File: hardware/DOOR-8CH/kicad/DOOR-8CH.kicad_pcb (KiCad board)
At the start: 4 copper layers, 260 x 160 mm, 230 parts, among them J1 FUSED_12V_CH1, J10 ACTUATOR_CH2, J11 ACTUATOR_CH3, J12 ACTUATOR_CH4, J13 ACTUATOR_CH5, J14 ACTUATOR_CH6, J15 ACTUATOR_CH7, J16 ACTUATOR_CH8, J2 FUSED_12V_CH2, J201 REED_A_OPEN_3V3_SIG_GND, J202 REED_A_CLOSED_3V3_SIG_GND, J203 REED_A_IN_PLACE_3V3_SIG_GND, J204 REED_B_OPEN_3V3_SIG_GND, J205 REED_B_CLOSED_3V3_SIG_GND, J206 REED_B_IN_PLACE_3V3_SIG_GND, J211 CAP_CS1_GND, J212 CAP_CS2_GND, J213 CAP_CS3_GND, J214 CAP_CS4_GND, J215 CAP_CS5_GND, J216 CAP_CS6_GND, J217 CAP_CS7_GND, J218 CAP_CS8_GND, J220 SWD_S1_3V3_DIO_CLK_NRST_GND, J230 LOGIC_12V_GND, J240 CANH_CANL_GND_SHIELD, J3 FUSED_12V_CH3, J4 FUSED_12V_CH4, J5 FUSED_12V_CH5, J6 FUSED_12V_CH6, J7 FUSED_12V_CH7, J8 FUSED_12V_CH8, J9 ACTUATOR_CH1, U1 VNH5019A-E, U2 VNH5019A-E, U230 AMS1117-3V3, U250 25LC256_SOIC8_CARRIER_ID, U3 VNH5019A-E, U4 VNH5019A-E, U5 VNH5019A-E, U6 VNH5019A-E, U7 VNH5019A-E, U8 VNH5019A-E

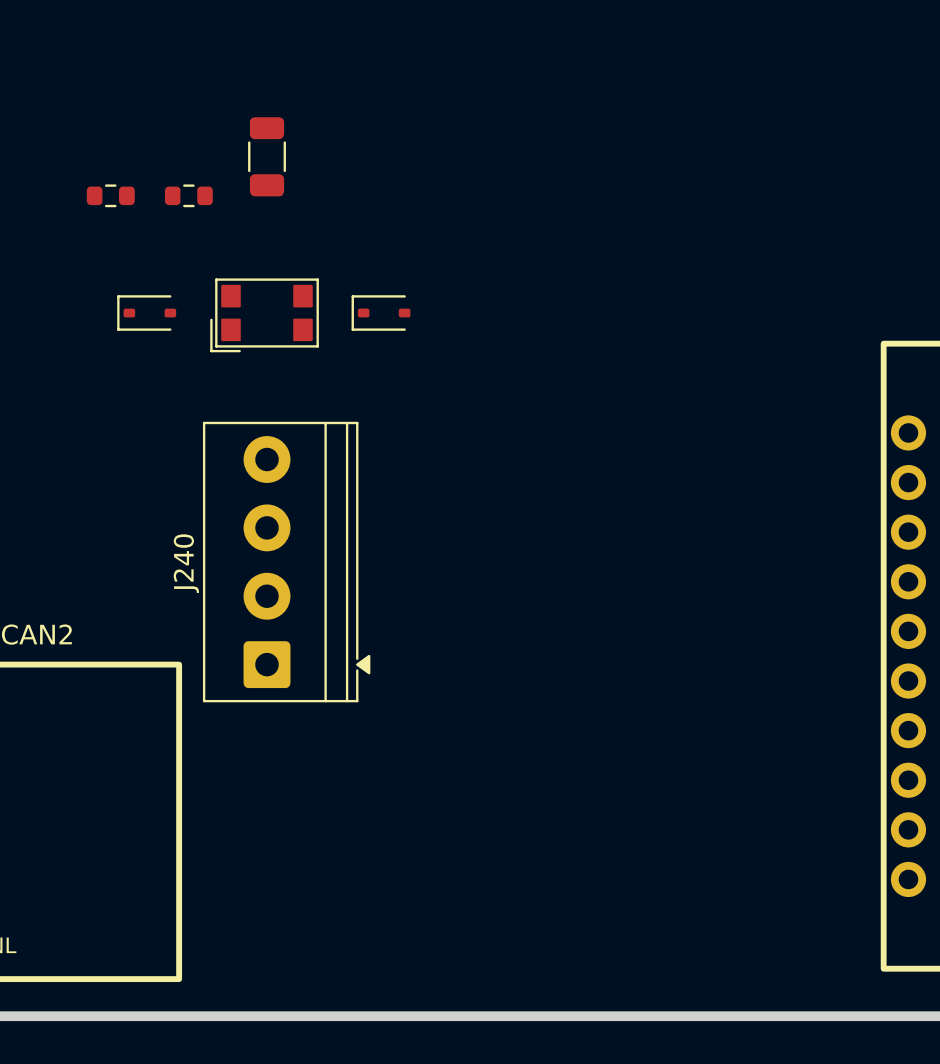
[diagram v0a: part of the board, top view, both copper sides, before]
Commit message: Compact CAN entry at board edge
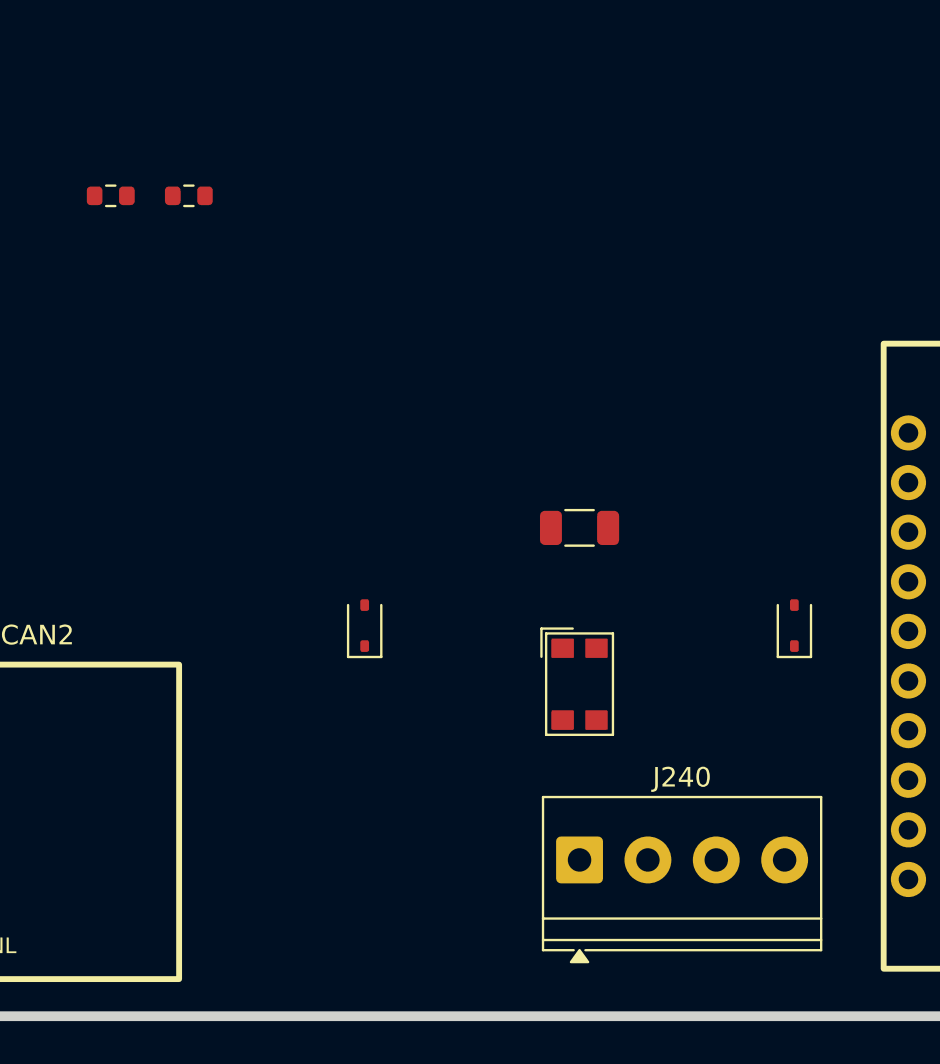
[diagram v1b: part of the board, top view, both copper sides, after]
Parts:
- moved D241 26.4 mm to (169.0, 140.0), turned to 90 degrees
- moved L240 24.8 mm to (158.0, 143.0), turned to 0 degrees
- moved R240 24.8 mm to (158.0, 135.0), turned to 0 degrees
- moved D240 19.4 mm to (147.0, 140.0), turned to 90 degrees
- moved J240 18.9 mm to (158.0, 152.0), turned to 0 degrees
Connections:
- D240 pad 1: CANH_BUS -> CANH_ENTRY
- D241 pad 1: CANL_BUS -> CANL_ENTRY

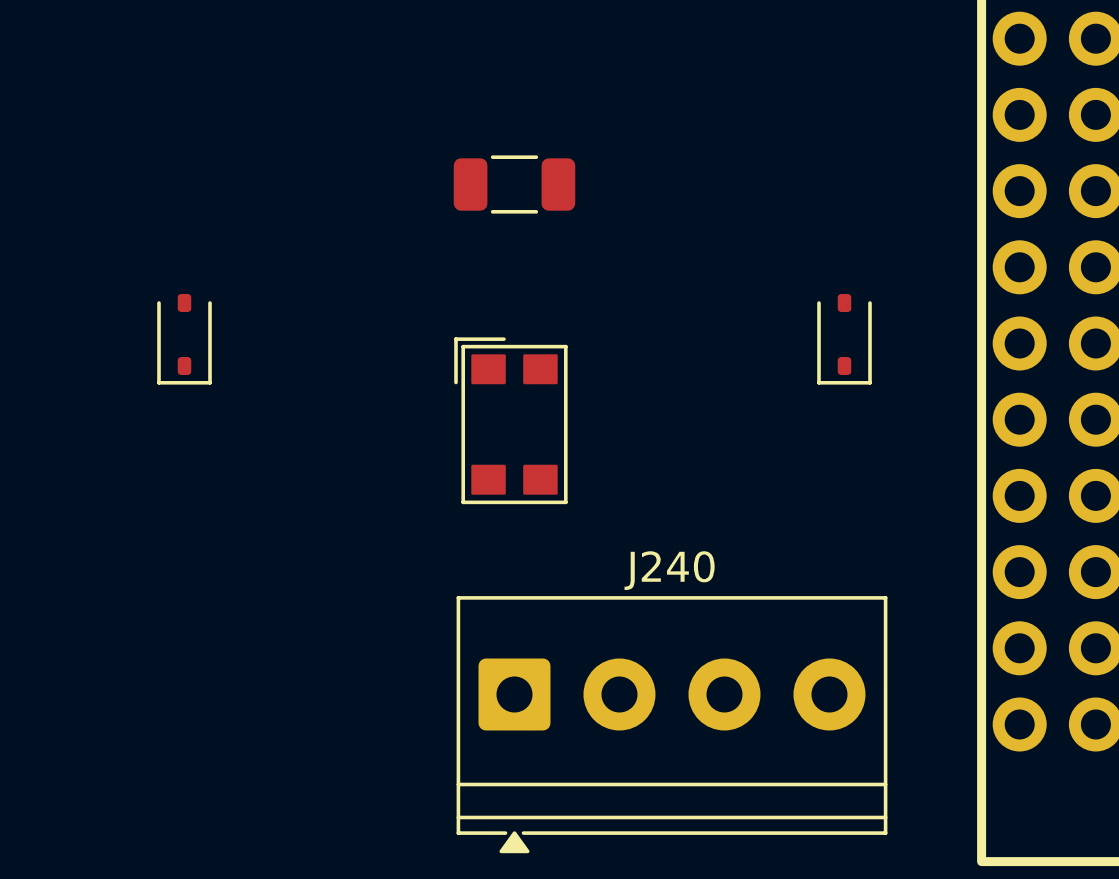
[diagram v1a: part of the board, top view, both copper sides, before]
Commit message: Route protected CAN entry
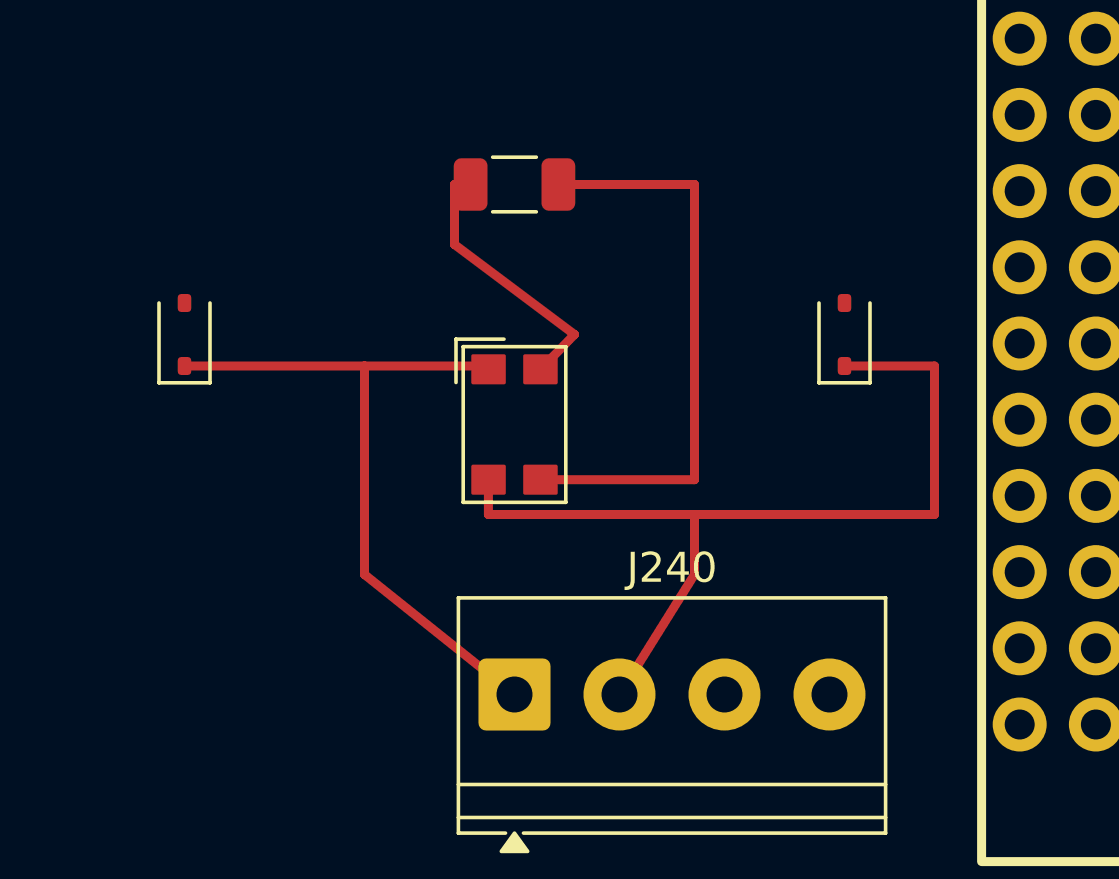
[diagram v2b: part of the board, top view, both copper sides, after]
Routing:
- net CANL_ENTRY: track 0.00 -> 30.7 mm
- net CANH_ENTRY: track 0.00 -> 23.6 mm
- net CANL_BUS: track 0.00 -> 19.5 mm
- net CANH_BUS: track 0.00 -> 9.16 mm

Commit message: Compact VNH power stage placement
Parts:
- moved C1702 28.6 mm to (191.0, 61.0)
- moved C1802 26.4 mm to (221.0, 61.0)
- moved C1102 26.0 mm to (9.00, 61.0)
- moved C1202 26.0 mm to (39.0, 61.0)
- moved C1302 26.0 mm to (69.0, 61.0)
- moved C1402 26.0 mm to (99.0, 61.0)
- moved C1502 26.0 mm to (131.0, 61.0)
- moved C1602 26.0 mm to (161.0, 61.0)
- moved C1301 24.0 mm to (69.0, 53.0)
- moved C1401 24.0 mm to (99.0, 53.0)
- moved C1501 24.0 mm to (131.0, 53.0)
- moved C1601 24.0 mm to (161.0, 53.0)
- moved C1101 22.1 mm to (9.00, 53.0)
- moved C1201 22.1 mm to (39.0, 53.0)
- moved C1701 21.0 mm to (191.0, 53.0)
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
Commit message: Route independent VNH supply feeds
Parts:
- moved HS8A 2.00 mm to (234.0, 22.0)
- moved HS8B 2.00 mm to (234.0, 48.0)
- moved U8 2.00 mm to (234.0, 35.0)
- turned C1101 to 180 degrees
- turned C1201 to 180 degrees
- turned C1301 to 180 degrees
- turned C1401 to 180 degrees
- turned C1501 to 180 degrees
- turned C1601 to 180 degrees
- turned C1701 to 180 degrees
- turned C1801 to 180 degrees
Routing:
- net FUSED_12V_CH7: track 0.00 -> 109.2 mm, vias 0 -> 3
- net FUSED_12V_CH6: track 0.00 -> 109.2 mm, vias 0 -> 3
- net FUSED_12V_CH5: track 0.00 -> 109.2 mm, vias 0 -> 3
- net FUSED_12V_CH4: track 0.00 -> 109.2 mm, vias 0 -> 3
- net FUSED_12V_CH3: track 0.00 -> 109.2 mm, vias 0 -> 3
- net FUSED_12V_CH2: track 0.00 -> 109.2 mm, vias 0 -> 3
- net FUSED_12V_CH1: track 0.00 -> 109.2 mm, vias 0 -> 3
- net FUSED_12V_CH8: track 0.00 -> 98.3 mm, vias 0 -> 3

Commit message: Add internal ground planes
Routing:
- added copper zone on In1.Cu, net GND
- added copper zone on In2.Cu, net GND
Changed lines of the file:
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@@
 		(net "CANL_BUS")
+	)
+	(zone
+		(net "GND")
+		(layer "In1.Cu")
+		(hatch edge 0.5)
+		(connect_pads
+			(clearance 0.3)
+		)
+		(min_thickness 0.25)
+		(fill yes
+			(thermal_gap 0.5)
+			(thermal_bridge_width 0.5)
+			(island_removal_mode 0)
+		)
+		(polygon
+			(pts
+				(xy 0.5 0.5) (xy 259.5 0.5) (xy 259.5 159.5) (xy 0.5 159.5)
+			)
+		)
+	)
+	(zone
+		(net "GND")
+		(layer "In2.Cu")
+		(hatch edge 0.5)
+		(connect_pads
+			(clearance 0.3)
+		)
+		(min_thickness 0.25)
+		(fill yes
+			(thermal_gap 0.5)
+			(thermal_bridge_width 0.5)
+			(island_removal_mode 0)
+		)
+		(polygon
+			(pts
+				(xy 0.5 0.5) (xy 259.5 0.5) (xy 259.5 159.5) (xy 0.5 159.5)
+			)
+		)
 	)
 	(embedded_fonts no)

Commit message: Route protected CAN trunk to both transceivers
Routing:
- net CANL_BUS: track 19.5 -> 257.4 mm, vias 0 -> 1
- net CANH_BUS: track 9.16 -> 246.3 mm, vias 0 -> 1
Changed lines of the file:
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@@
-	)
-	(segment
-		(start 156 135)
-		(end 156.54 135)
-		(width 0.3)
-		(layer "F.Cu")
-		(net "CANH_BUS")
 	)
 	(segment
@@
 	)
 	(segment
+		(start 156 135)
+		(end 156.54 135)
+		(width 0.3)
+		(layer "F.Cu")
+		(net "CANH_BUS")
+	)
+	(segment
 		(start 156 137)
 		(end 156 135)
@@
 		(net "CANH_BUS")
 	)
+	(via
+		(at 160 140)
+		(size 0.8)
+		(drill 0.35)
+		(layers "F.Cu" "B.Cu")
+		(net "CANH_BUS")
+	)
 	(segment
-		(start 164 135)
+		(start 128 110)
+		(end 128 153.86)
+		(width 0.3)
+		(layer "In1.Cu")
+		(net "CANH_BUS")
+	)
+	(segment
+		(start 128 153.86)
+		(end 124.27 153.86)
+		(width 0.3)
+		(layer "In1.Cu")
+		(net "CANH_BUS")
+	)
+	(segment
+		(start 160 140)
+		(end 148 140)
+		(width 0.3)
+		(layer "In1.Cu")
+		(net "CANH_BUS")
+	)
+	(segment
+		(start 148 140)
+		(end 148 110)
+		(width 0.3)
+		(layer "In1.Cu")
+		(net "CANH_BUS")
+	)
+	(segment
+		(start 68 153.86)
+		(end 64.269999 153.86)
+		(width 0.3)
+		(layer "In1.Cu")
+		(net "CANH_BUS")
+	)
+	(segment
+		(start 68 110)
+		(end 68 153.86)
+		(width 0.3)
+		(layer "In1.Cu")
+		(net "CANH_BUS")
+	)
+	(segment
+		(start 148 110)
+		(end 68 110)
+		(width 0.3)
+		(layer "In1.Cu")
+		(net "CANH_BUS")
+	)
+	(segment
+		(start 148 110)
+		(end 128 110)
+		(width 0.3)
+		(layer "In1.Cu")
+		(net "CANH_BUS")
+	)
+	(segment
+		(start 158.87 144.84)
+		(end 162 143)
+		(width 0.3)
+		(layer "F.Cu")
+		(net "CANL_BUS")
+	)
+	(segment
+		(start 162 135)
 		(end 159.46 135)
 		(width 0.3)
@@
 	)
 	(segment
-		(start 158.87 144.84)
-		(end 164 144.84)
+		(start 162 143)
+		(end 162 135)
 		(width 0.3)
 		(layer "F.Cu")
 		(net "CANL_BUS")
 	)
-	(segment
-		(start 164 144.84)
-		(end 164 135)
-		(width 0.3)
-		(layer "F.Cu")
+	(via
+		(at 162 143)
+		(size 0.8)
+		(drill 0.35)
+		(layers "F.Cu" "B.Cu")
 		(net "CANL_BUS")
 	)
+	(segment
+		(start 162 143)
+		(end 155 143)
+		(width 0.3)
+		(layer "In2.Cu")
+		(net "CANL_BUS")
+	)
+	(segment
+		(start 155 143)
+		(end 155 112)
+		(width 0.3)
+		(layer "In2.Cu")
+		(net "CANL_BUS")
+	)
+	(segment
+		(start 70 156.4)
+		(end 64.269999 156.4)
+		(width 0.3)
+		(layer "In2.Cu")
+		(net "CANL_BUS")
+	)
+	(segment
+		(start 155 112)
+		(end 70 112)
+		(width 0.3)
+		(layer "In2.Cu")
+		(net "CANL_BUS")
+	)
+	(segment
+		(start 70 112)
+		(end 70 156.4)
+		(width 0.3)
+		(layer "In2.Cu")
+		(net "CANL_BUS")
+	)
+	(segment
+		(start 140 112)
+		(end 140 156.4)
+		(width 0.3)
+		(layer "In2.Cu")
+		(net "CANL_BUS")
+	)
+	(segment
+		(start 150 112)
+		(end 140 112)
+		(width 0.3)
+		(layer "In2.Cu")
+		(net "CANL_BUS")
+	)
+	(segment
+		(start 140 156.4)
+		(end 124.27 156.4)
+		(width 0.3)
+		(layer "In2.Cu")
+		(net "CANL_BUS")
+	)

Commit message: Route STM32 CAN1 control signals
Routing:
- net S1_CAN_RX: track 0.00 -> 72.6 mm
- net S1_CAN_TX: track 0.00 -> 46.0 mm
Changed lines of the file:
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@@
+	)
+	(segment
+		(start 42 150)
+		(end 42 158)
+		(width 0.25)
+		(layer "B.Cu")
+		(net "S1_CAN_TX")
+	)
+	(segment
+		(start 37.38 145.38)
+		(end 42 150)
+		(width 0.25)
+		(layer "B.Cu")
+		(net "S1_CAN_TX")
+	)
+	(segment
+		(start 60 158)
+		(end 60 148.78)
+		(width 0.25)
+		(layer "B.Cu")
+		(net "S1_CAN_TX")
+	)
+	(segment
+		(start 60 148.78)
+		(end 64.269999 148.78)
+		(width 0.25)
+		(layer "B.Cu")
+		(net "S1_CAN_TX")
+	)
+	(segment
+		(start 42 158)
+		(end 60 158)
+		(width 0.25)
+		(layer "B.Cu")
+		(net "S1_CAN_TX")
+	)
+	(segment
+		(start 30 152.5)
+		(end 30 159)
+		(width 0.25)
+		(layer "B.Cu")
+		(net "S1_CAN_RX")
+	)
+	(segment
+		(start 30 159)
+		(end 73 159)
+		(width 0.25)
+		(layer "B.Cu")
+		(net "S1_CAN_RX")
+	)
+	(segment
+		(start 73 159)
+		(end 73 151.32)
+		(width 0.25)
+		(layer "B.Cu")
+		(net "S1_CAN_RX")
+	)
+	(segment
+		(start 73 151.32)
+		(end 64.269999 151.32)
+		(width 0.25)
+		(layer "B.Cu")
+		(net "S1_CAN_RX")
+	)
+	(segment
+		(start 34.84 147.92)
+		(end 30 152.5)
+		(width 0.25)
+		(layer "B.Cu")
+		(net "S1_CAN_RX")
 	)
 	(segment

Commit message: Route ESP32 CAN2 control signals
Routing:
- net ESP_CAN_TX_GPIO39: track 0.00 -> 257.0 mm, vias 0 -> 1
- net ESP_CAN_RX_GPIO38: track 0.00 -> 205.9 mm
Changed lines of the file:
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@@
+	)
+	(segment
+		(start 137 151.32)
+		(end 124.27 151.32)
+		(width 0.25)
+		(layer "B.Cu")
+		(net "ESP_CAN_RX_GPIO38")
+	)
+	(segment
+		(start 30.86 82.14)
+		(end 35 78)
+		(width 0.25)
+		(layer "B.Cu")
+		(net "ESP_CAN_RX_GPIO38")
+	)
+	(segment
+		(start 137 72)
+		(end 137 151.32)
+		(width 0.25)
+		(layer "B.Cu")
+		(net "ESP_CAN_RX_GPIO38")
+	)
+	(segment
+		(start 35 72)
+		(end 137 72)
+		(width 0.25)
+		(layer "B.Cu")
+		(net "ESP_CAN_RX_GPIO38")
+	)
+	(segment
+		(start 35 78)
+		(end 35 72)
+		(width 0.25)
+		(layer "B.Cu")
+		(net "ESP_CAN_RX_GPIO38")
+	)
+	(segment
+		(start 145 148.78)
+		(end 124.27 148.78)
+		(width 0.25)
+		(layer "F.Cu")
+		(net "ESP_CAN_TX_GPIO39")
+	)
+	(via
+		(at 145 148.78)
+		(size 0.8)
+		(drill 0.35)
+		(layers "F.Cu" "B.Cu")
+		(net "ESP_CAN_TX_GPIO39")
+	)
+	(segment
+		(start 28.32 82.14)
+		(end 28.32 78)
+		(width 0.25)
+		(layer "B.Cu")
+		(net "ESP_CAN_TX_GPIO39")
+	)
+	(segment
+		(start 145 64)
+		(end 145 148.78)
+		(width 0.25)
+		(layer "B.Cu")
+		(net "ESP_CAN_TX_GPIO39")
+	)
+	(segment
+		(start 20 64)
+		(end 145 64)
+		(width 0.25)
+		(layer "B.Cu")
+		(net "ESP_CAN_TX_GPIO39")
+	)
+	(segment
+		(start 28.32 78)
+		(end 20 78)
+		(width 0.25)
+		(layer "B.Cu")
+		(net "ESP_CAN_TX_GPIO39")
+	)
+	(segment
+		(start 20 78)
+		(end 20 64)
+		(width 0.25)
+		(layer "B.Cu")
+		(net "ESP_CAN_TX_GPIO39")
 	)
 	(segment
